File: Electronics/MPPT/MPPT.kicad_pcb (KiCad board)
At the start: 2 copper layers, 172.7 x 116.8 mm, 132 parts, among them J1 Solar Array, J2 Battery, J3 Car Power, J4 CAN_In, J5 CAN_Out, Q1 200N25N, Q2 200N25N, SW1 RESET, SW2 CAN Address, U1 PQMC3-D12-S9-S, U2 Nucleo_L432KC, U3 UCC37321, U4 INA210, U5 ADM3055E, U6 INA210, U7 CDSOT23-T24CAN

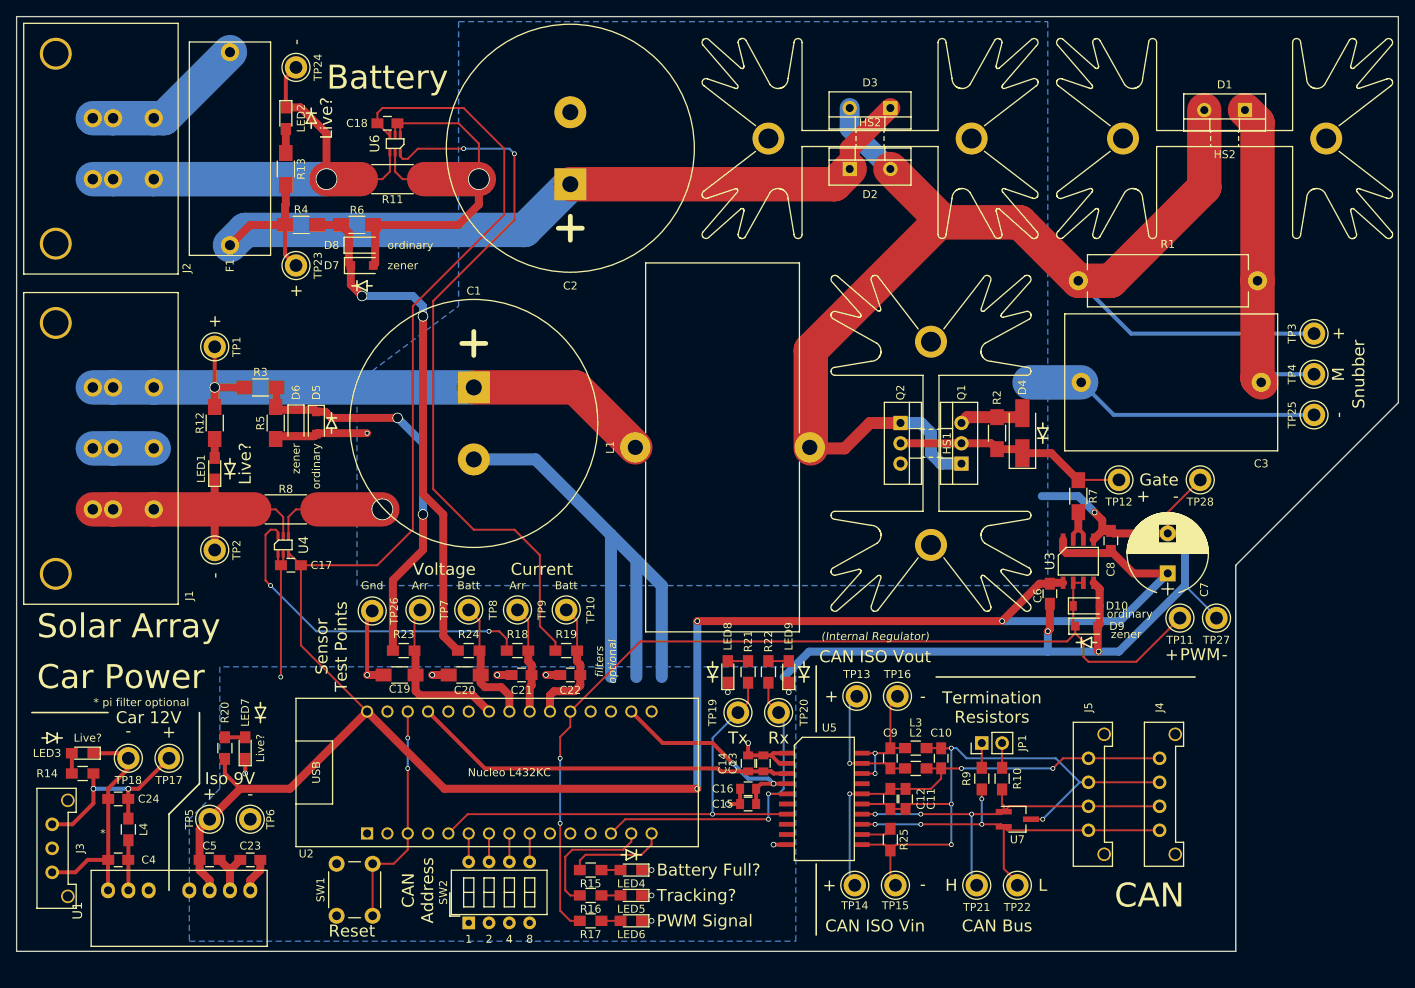
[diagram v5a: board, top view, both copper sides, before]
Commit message: MPPT: Add mounting holes in approximate four corners of board.
I needed to nudge and reroute a few things to accomplish this, but nothing vital has changed.
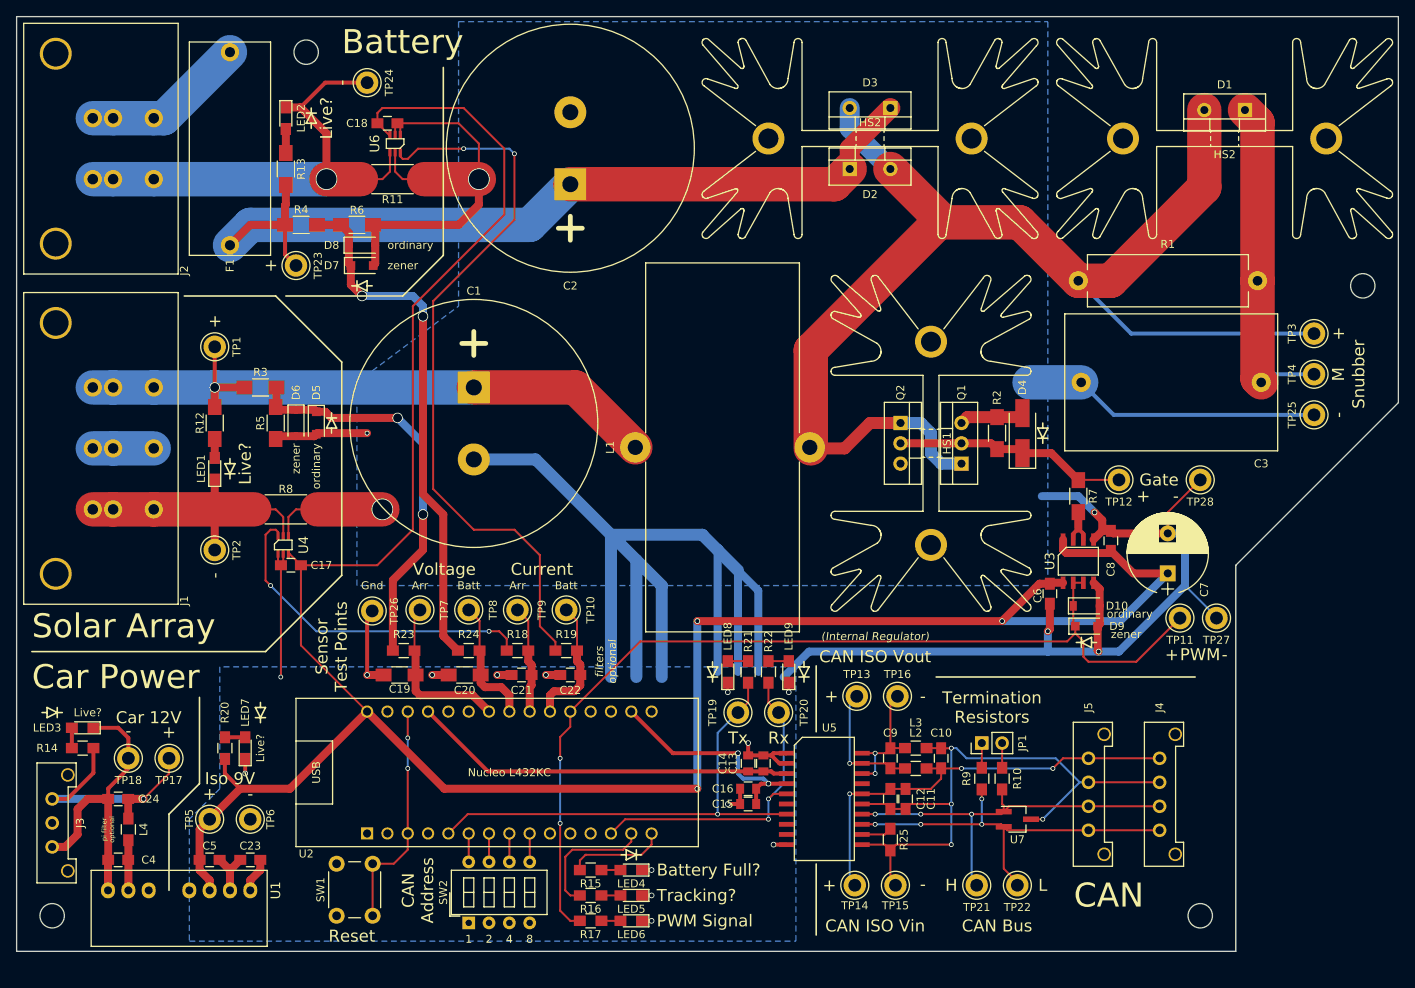
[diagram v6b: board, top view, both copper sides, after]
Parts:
- added REF**: MountingHole_4-40_PanHead, UTSVT_Mechanical:MountingHole_4-40_PanHead, F.Cu at (67.3, 35.6)
- added REF**: MountingHole_4-40_PanHead, UTSVT_Mechanical:MountingHole_4-40_PanHead, F.Cu at (199.4, 64.8)
- added REF**: MountingHole_4-40_PanHead, UTSVT_Mechanical:MountingHole_4-40_PanHead, F.Cu at (35.6, 143.5)
- added REF**: MountingHole_4-40_PanHead, UTSVT_Mechanical:MountingHole_4-40_PanHead, F.Cu at (179.1, 143.5)
- moved TP24 9.09 mm to (74.9, 39.4)
- moved J3 3.18 mm to (35.6, 128.9)
- moved LED3 3.17 mm to (39.4, 120.0)
- moved R14 3.17 mm to (39.4, 122.6)
- moved REF** 3.17 mm to (35.6, 118.1)
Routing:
- net GNDPWR: track 373.6 -> 433.0 mm
- net +12V: track 24.8 -> 31.8 mm, vias 2 -> 1
- net GNDREF: track 29.8 -> 36.3 mm
- net /-Batt: track 57.6 -> 61.7 mm
- net +3V3: track 27.5 -> 28.4 mm
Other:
- board text added: "pi filter optional"
- board text removed: "*"
- board text removed: "* pi filter optional"
